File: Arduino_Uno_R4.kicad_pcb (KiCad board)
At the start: 2 copper layers, 48.9 x 38.1 mm, 55 parts, among them J1 Jack-DC, J17 ICSP1, J2 ICSP2, J3 USB_B, J4 PORTB, J5 PWR_PORT, J6 PORTC, J7 PORTD, Q1 FDN340P, SW1 RES, U1 LMV358, U2 LP2985-3.3, U3 NCP1117ST50, U5 ATmega16U2-MU, U6 ATmega328P-MU, Y1 16MHz, Y2 16MHz

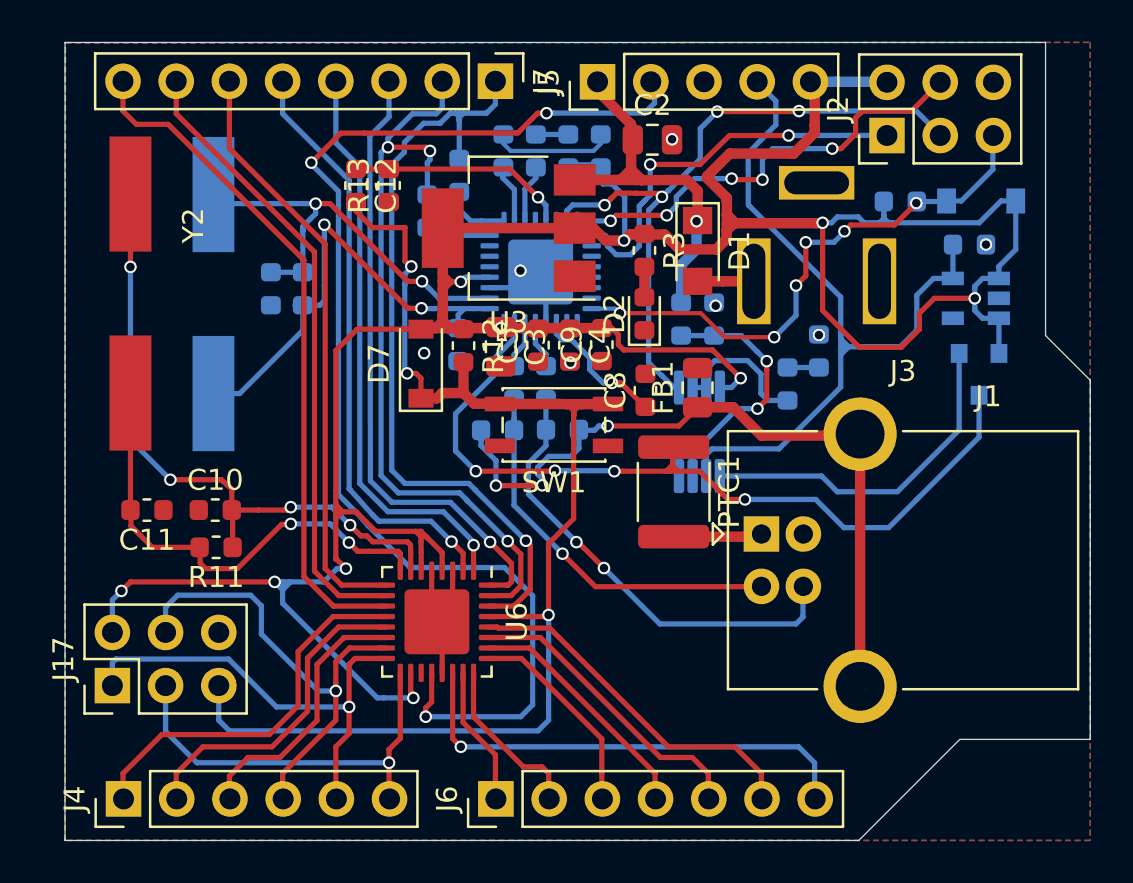
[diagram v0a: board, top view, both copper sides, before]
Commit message: Improved readability, fixed component reference positions, added text for IO ports
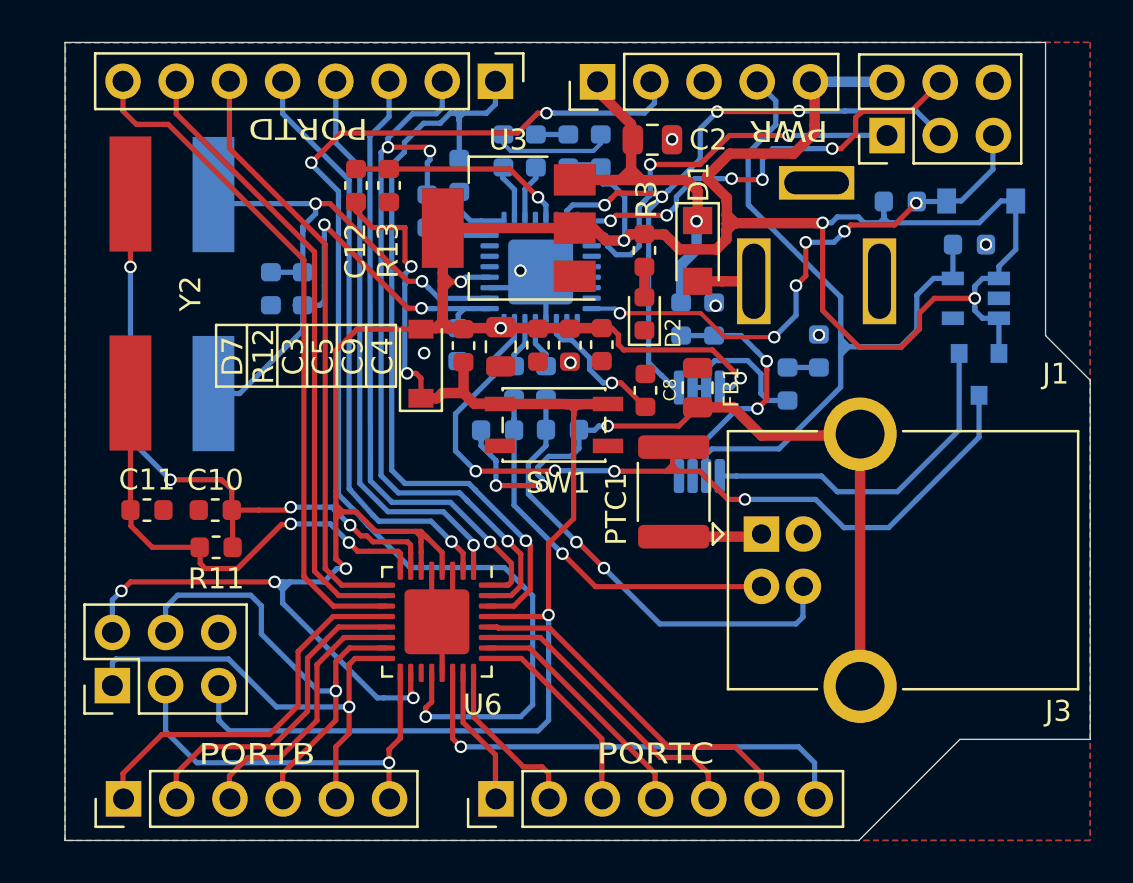
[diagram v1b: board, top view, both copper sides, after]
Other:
- board text added: "PORTB"
- board text added: "PORTC"
- board text added: "PORTD"
- board text added: "PWR"

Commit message: Improved consistency of component label positioning, added a couple descriptive labels
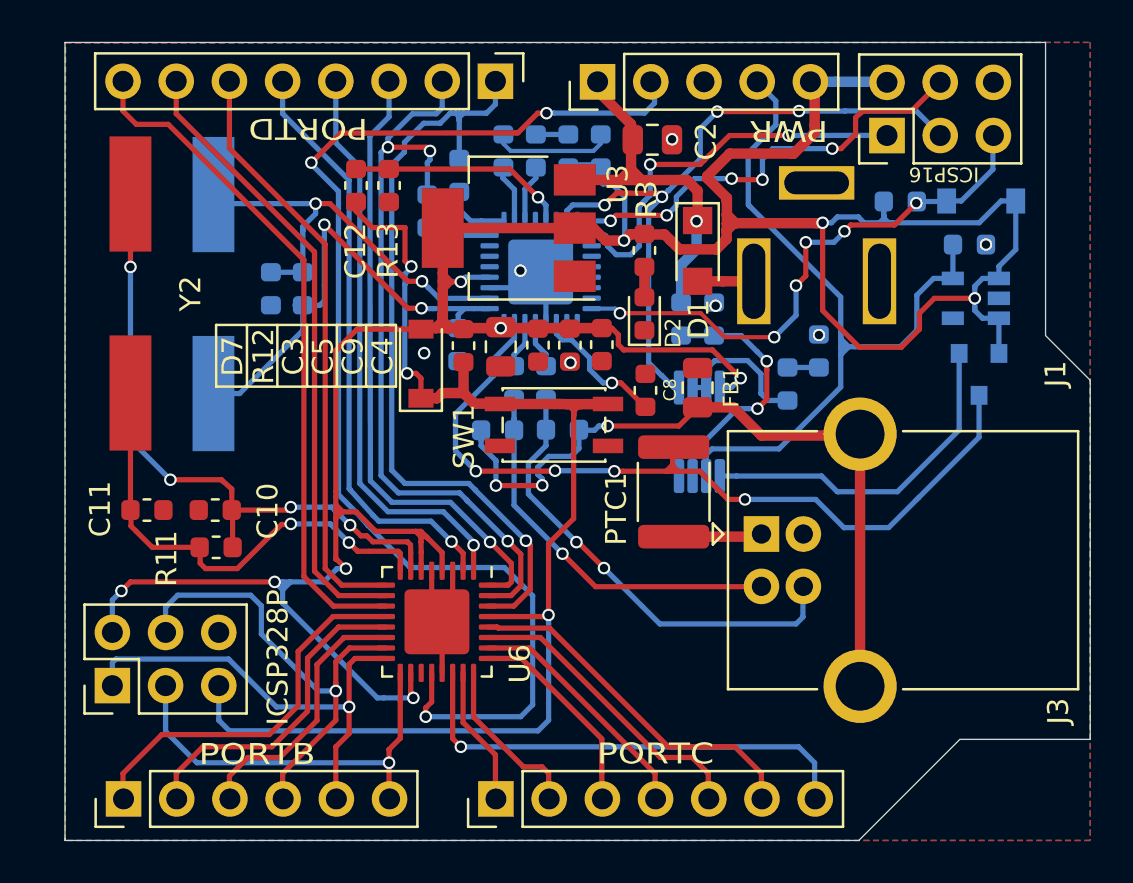
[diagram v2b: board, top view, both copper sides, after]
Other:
- board text added: "ICSP16"
- board text added: "ICSP328P"

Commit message: Generated GERBER and drill files
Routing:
- net Net-(C12-Pad2): track 60.4 -> 59.4 mm
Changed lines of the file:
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@@
     (thickness 1.6)
     (drawings 24)
-    (tracks 860)
+    (tracks 858)
     (zones 0)
     (modules 55)
@@
     (0 F.Cu signal)
     (31 B.Cu signal)
-    (34 B.Paste user)
-    (35 F.Paste user)
     (36 B.SilkS user)
     (37 F.SilkS user)
     (38 B.Mask user)
     (39 F.Mask user)
-    (40 Dwgs.User user)
+    (40 Dwgs.User user hide)
     (44 Edge.Cuts user)
-    (45 Margin user)
-    (46 B.CrtYd user)
-    (47 F.CrtYd user)
-    (48 B.Fab user)
-    (49 F.Fab user)
+    (45 Margin user hide)
+    (46 B.CrtYd user hide)
+    (47 F.CrtYd user hide)
+    (48 B.Fab user hide)
+    (49 F.Fab user hide)
   )
   (setup
@@
     (visible_elements 7FFFFFFF)
     (pcbplotparams
-      (layerselection 0x010fc_ffffffff)
+      (layerselection 0x010f0_ffffffff)
       (usegerberextensions false)
       (usegerberattributes false)
@@
       (outputformat 1)
       (mirror false)
-      (drillshape 1)
+      (drillshape 0)
       (scaleselection 1)
       (outputdirectory ""))
@@
   (segment (start 72.009 75.7174) (end 72.644 75.7174) (width 0.5) (layer F.Cu) (net 8))
   (segment (start 72.644 75.7174) (end 73.898 75.708) (width 0.5) (layer F.Cu) (net 8))
-  (segment (start 63.837736 67.2846) (end 64.262 67.2846) (width 0.25) (layer F.Cu) (net 8))
-  (segment (start 62.7069 67.2846) (end 63.837736 67.2846) (width 0.25) (layer F.Cu) (net 8))
-  (segment (start 61.9252 66.5029) (end 62.7069 67.2846) (width 0.25) (layer F.Cu) (net 8))
-  (segment (start 61.9252 66.0654) (end 61.9252 66.5029) (width 0.25) (layer F.Cu) (net 8))
   (segment (start 64.252 70.0024) (end 64.262 69.9924) (width 0.25) (layer B.Cu) (net 8))
   (via (at 64.564242 69.141358) (size 0.6) (drill 0.4) (layers F.Cu B.Cu) (net 8))
-  (segment (start 64.262 67.2846) (end 64.262 68.8848) (width 0.25) (layer F.Cu) (net 8))
-  (segment (start 64.262 68.8848) (end 64.5668 69.1896) (width 0.25) (layer F.Cu) (net 8))
   (segment (start 64.262 69.4944) (end 64.262 69.9924) (width 0.25) (layer B.Cu) (net 8))
   (segment (start 64.5668 69.1896) (end 64.262 69.4944) (width 0.25) (layer B.Cu) (net 8))
+  (segment (start 61.9252 66.5029) (end 61.9252 66.0654) (width 0.25) (layer F.Cu) (net 8))
+  (segment (start 64.262 68.8397) (end 61.9252 66.5029) (width 0.25) (layer F.Cu) (net 8))
+  (segment (start 64.262584 68.8397) (end 64.262 68.8397) (width 0.25) (layer F.Cu) (net 8))
+  (segment (start 64.564242 69.141358) (end 64.262584 68.8397) (width 0.25) (layer F.Cu) (net 8))
   (segment (start 75.692 69.1642) (end 75.692 70.5866) (width 0.5) (layer F.Cu) (net 9))
   (segment (start 82.4992 73.9648) (end 84.1248 73.9648) (width 0.25) (layer B.Cu) (net 10))
